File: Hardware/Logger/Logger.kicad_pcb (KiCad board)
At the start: 2 copper layers, 70 x 71 mm, 89 parts, among them CN1 Conn_02x19_Odd_Even, CN10 Conn_02x19_Odd_Even, CN2 Conn_02x19_Odd_Even, CN7 Conn_02x19_Odd_Even, J1 Conn_Coaxial, J10 Conn_01x08_Female, J2 Conn_Coaxial, J3 Conn_Coaxial, J4 Conn_Coaxial, J5 USB_B_Micro, J6 112K-TAA0-RA1_ATTEND, J7 DB9_Female_MountingHoles, J8 Conn_01x06_Female, J9 Conn_01x08_Female, Q1 FDV304P, Q2 FDV304P, Q3 FDV304P, Q4 FDV304P, Q5 BC848, Q6 BC848, Q7 BC848, Q8 BC848, SW1 SW_Push, SW2 SW_Push, SW3 SW_Push, SW4 SW_Push, U1 ESP-12E, U2 ST7735S, U3 LD1117ASTR

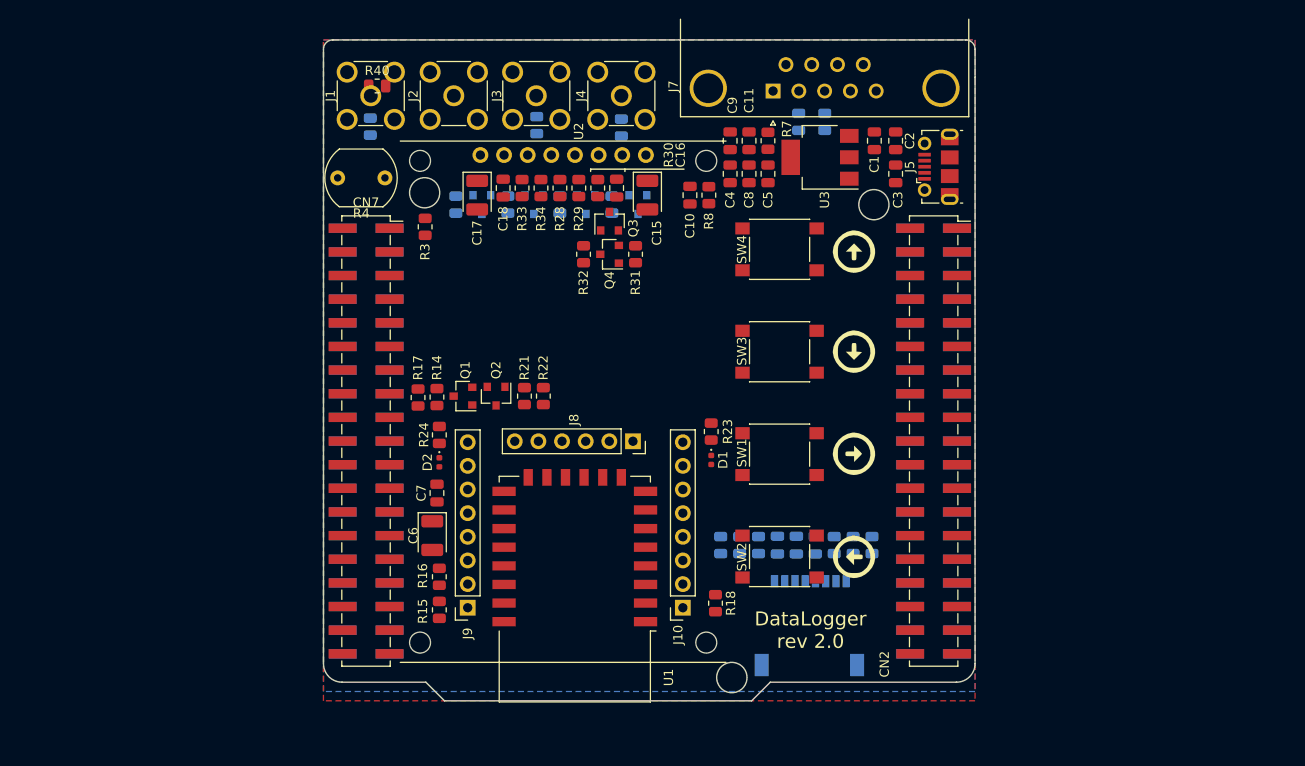
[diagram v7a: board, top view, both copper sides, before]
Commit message: PoC of esp32 support (setting esp32 to flashing mode))
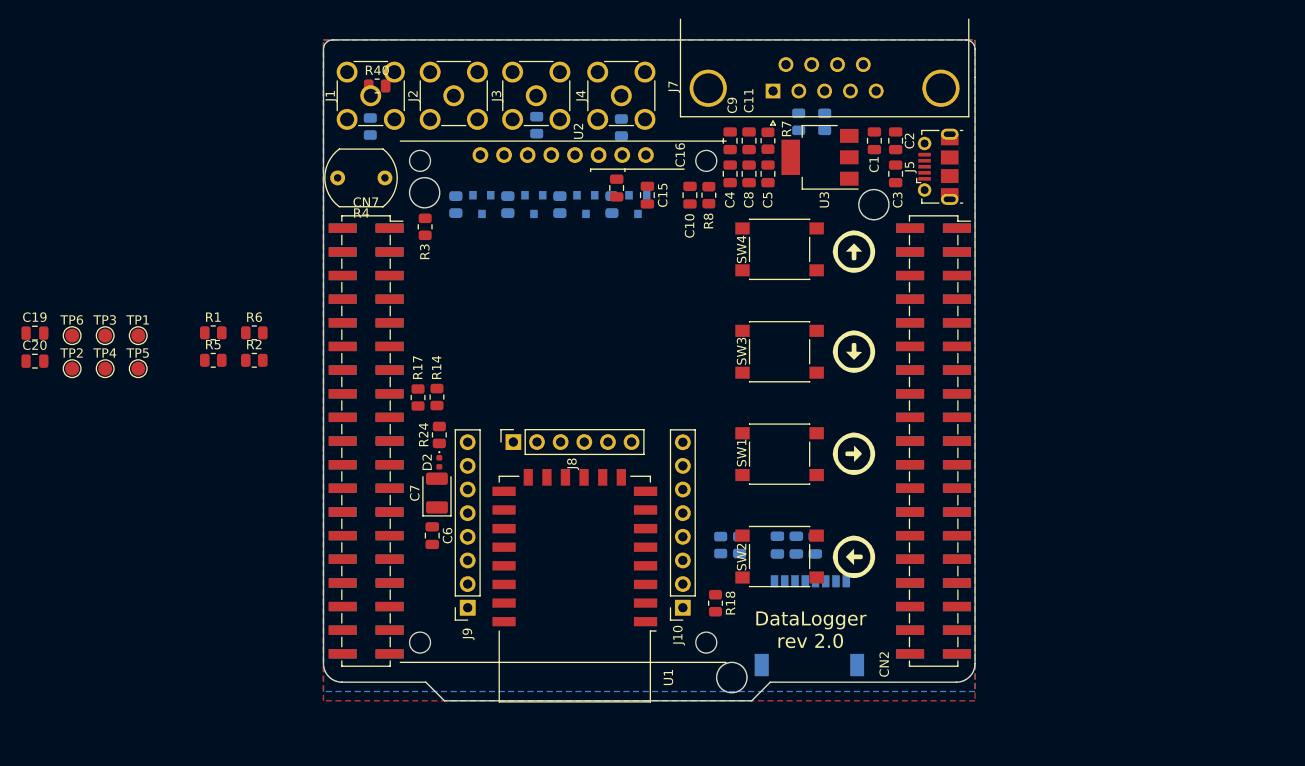
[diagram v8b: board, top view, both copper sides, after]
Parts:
- removed C17: 47u/6V3, Capacitor_Tantalum_SMD:CP_EIA-3528-21_Kemet-B
- removed C18: 100n, Capacitor_SMD:C_0805_2012Metric
- removed D1: LED, LED_SMD:LED_0402_1005Metric
- removed Q1, Q2, Q3, Q4: FDV304P, Package_TO_SOT_SMD:SOT-23
- removed R15, R16, R29, R30, R33, R34: 0R, Resistor_SMD:R_0805_2012Metric
- removed R20, R25, R26, R27: 10k, Resistor_SMD:R_0805_2012Metric
- removed R21, R22, R28, R31, R32: 1k, Resistor_SMD:R_0805_2012Metric
- removed R23: 120R, Resistor_SMD:R_0805_2012Metric
- added C19: 330n, Capacitor_SMD:C_0805_2012Metric, F.Cu at (99.0, 82.5)
- added C20: 330n, Capacitor_SMD:C_0805_2012Metric, F.Cu at (99.0, 85.5)
- added R1: 47R, Resistor_SMD:R_0805_2012Metric, F.Cu at (118.2, 82.5)
- added R2: 47R, Resistor_SMD:R_0805_2012Metric, F.Cu at (122.6, 85.4)
- added R5: 47R, Resistor_SMD:R_0805_2012Metric, F.Cu at (118.2, 85.4)
- added R6: 47R, Resistor_SMD:R_0805_2012Metric, F.Cu at (122.6, 82.5)
- added TP1: TestPoint, TestPoint:TestPoint_Pad_D1.5mm, F.Cu at (110.1, 82.8)
- added TP2: TestPoint, TestPoint:TestPoint_Pad_D1.5mm, F.Cu at (103.0, 86.3)
- added TP3: TestPoint, TestPoint:TestPoint_Pad_D1.5mm, F.Cu at (106.5, 82.8)
- added TP4: TestPoint, TestPoint:TestPoint_Pad_D1.5mm, F.Cu at (106.5, 86.3)
- added TP5: TestPoint, TestPoint:TestPoint_Pad_D1.5mm, F.Cu at (110.1, 86.3)
- added TP6: TestPoint, TestPoint:TestPoint_Pad_D1.5mm, F.Cu at (103.0, 82.8)
- C15, C6: value 47u/6V3 -> 100n; footprint Capacitor_Tantalum_SMD:CP_EIA-3528-21_Kemet-B -> Capacitor_SMD:C_0805_2012Metric
- C16: value 100n -> 470p
- C7: value 100n -> 47u/6V3; footprint Capacitor_SMD:C_0805_2012Metric -> Capacitor_Tantalum_SMD:CP_EIA-3528-21_Kemet-B
- R24: value 120R -> 470R
- moved J8 12.8 mm to (150.4, 94.2), turned to 90 degrees
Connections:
- net /WiFiInterface/ADC renamed /WiFiInterface/ESP_ADC
- net ESP_FLASH_MODE renamed ESP32_FLASH_MODE
- C15 pad 1: /UserInterface/LCD_BACKLIGHT -> /WiFiInterface/EN
- C16 pad 1: /UserInterface/LCD_BACKLIGHT -> ESP32_RST
- C6 pad 1: /WiFiInterface/ESP_VCC -> 3V3
- C7 pad 1: /WiFiInterface/ESP_VCC -> 3V3
- CN10 pad 14: ESP_TX -> ESP32_TX
- CN10 pad 16: ESP_RX -> ESP32_RX
- CN2 pad 13: ESP_TX -> ESP32_TX
- CN2 pad 15: ESP_RX -> ESP32_RX
- D2 pad 2: /WiFiInterface/GPIO15 -> /WiFiInterface/GPIO13
- J10 pad 1: /WiFiInterface/RST -> ESP32_RST
- J10 pad 8: /WiFiInterface/ESP_VCC -> 3V3
- J6 pad 1: Net-(J6-Pad1) -> (no net)
- J6 pad 2: CS_SD -> Net-(J6-Pad2)
- J6 pad 3: MOSI -> Net-(J6-Pad3)
- J6 pad 5: SCK -> Net-(J6-Pad5)
- J6 pad 7: MISO -> Net-(J6-Pad7)
- J6 pad 8: Net-(J6-Pad8) -> (no net)
- J8 pad 1: CS_ESP -> /WiFiInterface/ESP32_SCLK
- J8 pad 2: MISO -> /WiFiInterface/ESP32_MOSI
- J8 pad 3: /WiFiInterface/GPIO9 -> /WiFiInterface/GPIO10
- J8 pad 4: /WiFiInterface/GPIO10 -> /WiFiInterface/GPIO9
- J8 pad 5: MOSI -> /WiFiInterface/ESP32_MISO
- J8 pad 6: SCK -> /WiFiInterface/ESP32_CS0
- J9 pad 1: /WiFiInterface/TXD -> ESP32_TX
- J9 pad 2: /WiFiInterface/RXD -> ESP32_RX
- J9 pad 6: /WiFiInterface/GPIO12 -> /WiFiInterface/GPIO2
- R13 pad 2: Net-(J6-Pad8) -> /WiFiInterface/GPIO2
- R14 pad 1: /WiFiInterface/ESP_VCC -> 3V3
- R17 pad 1: /WiFiInterface/ESP_VCC -> 3V3
- R18 pad 1: /WiFiInterface/ESP_VCC -> 3V3
- R18 pad 2: /WiFiInterface/RST -> ESP32_RST
- R19 pad 1: 3V3 -> /WiFiInterface/GPIO15
- R19 pad 2: MISO -> GND
- U1 pad 1: /WiFiInterface/RST -> ESP32_RST
- U1 pad 10: MISO -> /WiFiInterface/ESP32_MISO
- U1 pad 13: MOSI -> /WiFiInterface/ESP32_MOSI
- U1 pad 14: SCK -> /WiFiInterface/ESP32_SCLK
- U1 pad 17: /WiFiInterface/GPIO12 -> /WiFiInterface/GPIO2
- U1 pad 21: /WiFiInterface/RXD -> ESP32_RX
- U1 pad 22: /WiFiInterface/TXD -> ESP32_TX
- U1 pad 8: /WiFiInterface/ESP_VCC -> 3V3
- U1 pad 9: CS_ESP -> /WiFiInterface/ESP32_CS0
- U2 pad 3: Net-(R33-Pad2) -> SCK
- U2 pad 4: Net-(R34-Pad2) -> MOSI
- U2 pad 5: Net-(R28-Pad2) -> RST_LCD
- U2 pad 6: Net-(R29-Pad2) -> DC_LCD
- U2 pad 7: Net-(R30-Pad2) -> CS_LCD
- U2 pad 8: /UserInterface/LCD_BACKLIGHT -> LCD_BRIGHT_PWM
